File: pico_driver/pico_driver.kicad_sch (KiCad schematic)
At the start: 20 parts, among them J1 GPIO, J2 SRV, J3 ESC, J4 ADC, J5 GP_Breakout, J6 VBUS_OUT, J7 3V3_OUT, J8 FUNC, SW1 SW_SPDT, SW2 SW_Push, SW3 SW_Push, U1 Pico

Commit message: update pcb layout
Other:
- company: (none) -> Engineering Physics - UCA
- title: BearCart - Cerebellum -> BearCart - Driver Board
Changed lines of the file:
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@@
 	(paper "USLetter")
 	(title_block
-		(title "BearCart - Cerebellum")
-		(date "2025-04-25")
-		(rev "0.2")
+		(title "BearCart - Driver Board")
+		(date "2025-05-09")
+		(rev "25.05.001")
+		(company "Engineering Physics - UCA")
 	)
 	(text "Additional pin functions:\nhttps://pinout.xyz/"

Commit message: update schemetic and pcb
Pin header for sw1
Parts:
- SW1: footprint Button_Switch_THT:SW_E-Switch_EG1271_SPDT -> Connector_PinHeader_2.54mm:PinHeader_1x03_P2.54mm_Vertical
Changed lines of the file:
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@@
 			)
 		)
-		(property "Footprint" "Button_Switch_THT:SW_E-Switch_EG1271_SPDT"
+		(property "Footprint" "Connector_PinHeader_2.54mm:PinHeader_1x03_P2.54mm_Vertical"
 			(at 135.89 133.35 0)
 			(effects

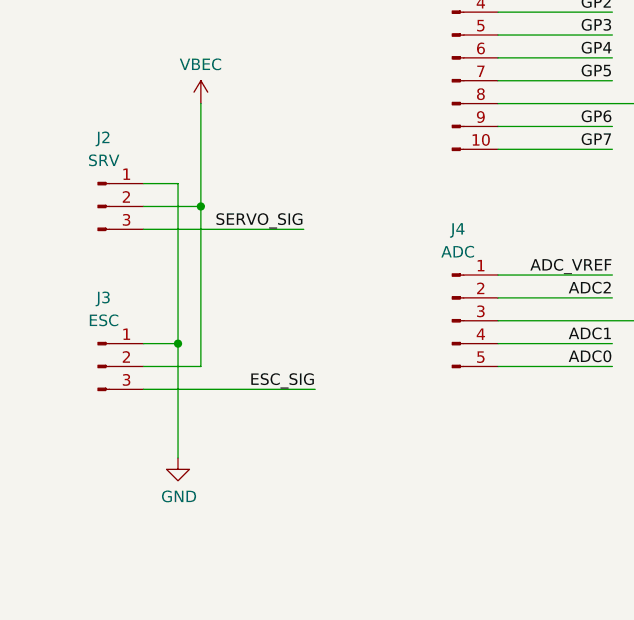
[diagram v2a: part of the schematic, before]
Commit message: update esc and servo pin layout
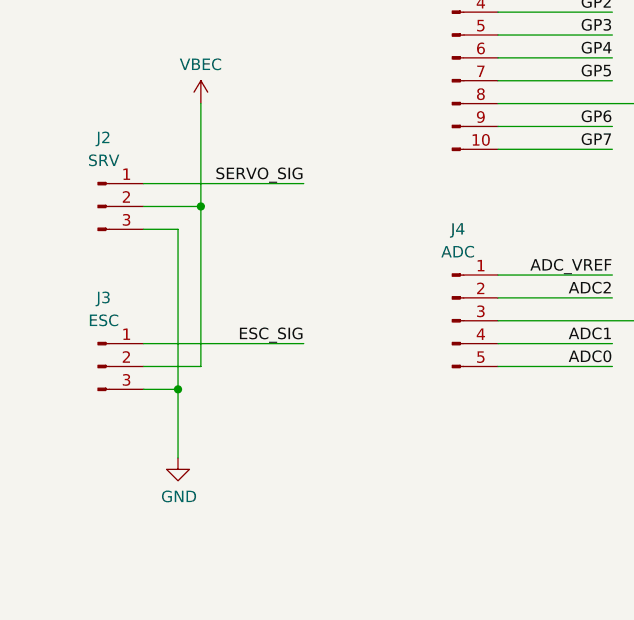
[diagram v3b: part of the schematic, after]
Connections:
- net ESC_SIG: now also J3.1 (Pin_1); no longer J3.3 (Pin_3)
- net GND: now also J2.3 (Pin_3), J3.3 (Pin_3); no longer J2.1 (Pin_1), J3.1 (Pin_1)
- net SERVO_SIG: now also J2.1 (Pin_1); no longer J2.3 (Pin_3)

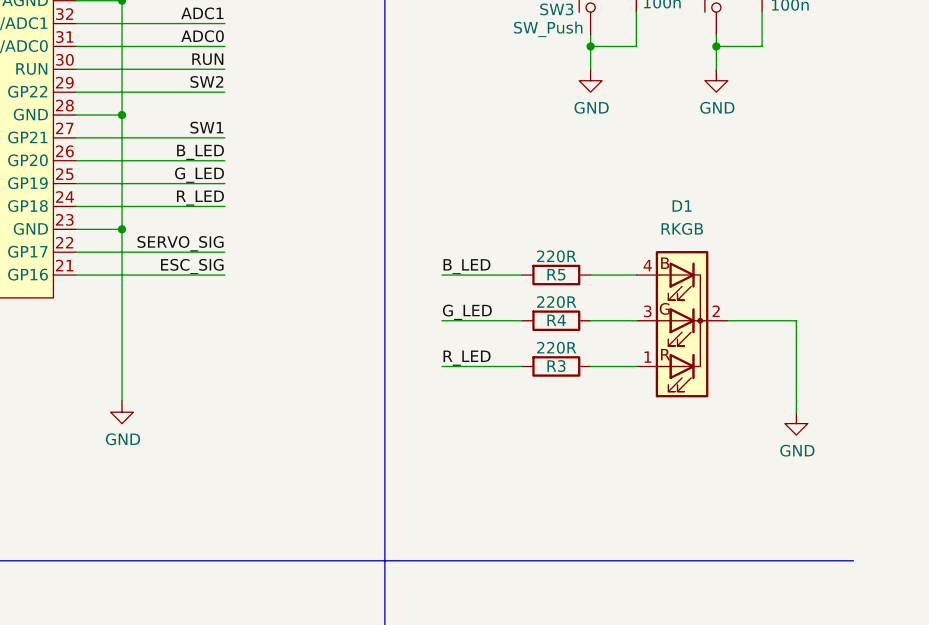
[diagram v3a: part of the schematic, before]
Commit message: update LED footprint
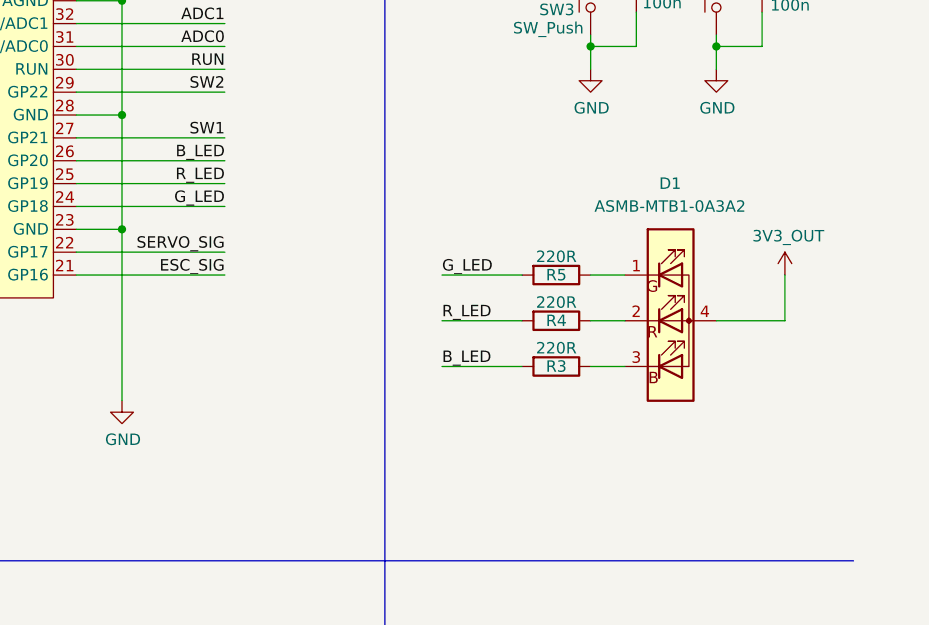
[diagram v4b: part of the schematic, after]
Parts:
- removed D1: RKGB, LED_THT:LED_D5.0mm-4_RGB_Wide_Pins, symbol Device:LED_RKGB
- added D1: ASMB-MTB1-0A3A2, LED_SMD:LED_Avago_PLCC4_3.2x2.8mm_CW, symbol RGB_PLCC4:ASMB-MTB1-0A3A2
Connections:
- net 3V3_OUT: now also D1.4 (A)
- net B_LED: now also R3.2; no longer R5.2
- net G_LED: now also R5.2, U1.24 (GP18); no longer R4.2, U1.25 (GP19)
- net R_LED: now also R4.2, U1.25 (GP19); no longer R3.2, U1.24 (GP18)
- net at R5.1: now also D1.1 (RK)
- net at R4.1: now also D1.2 (GK)
- net at R3.1: now also D1.3 (BK)

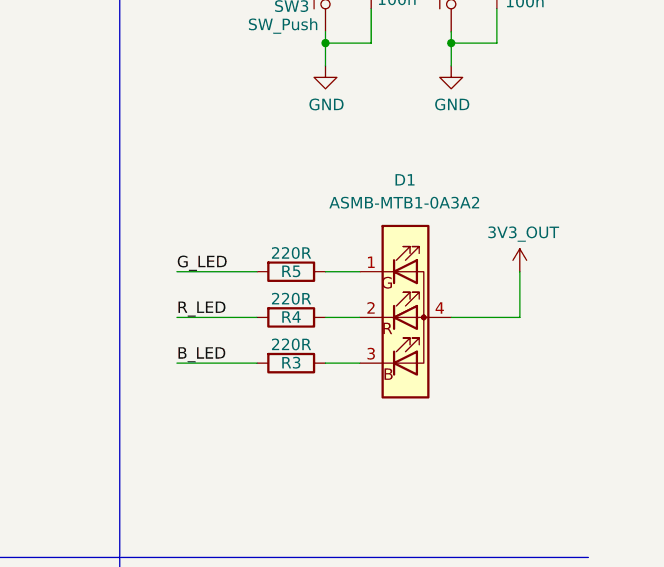
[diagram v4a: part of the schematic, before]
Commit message: update rgb led footprint and layout
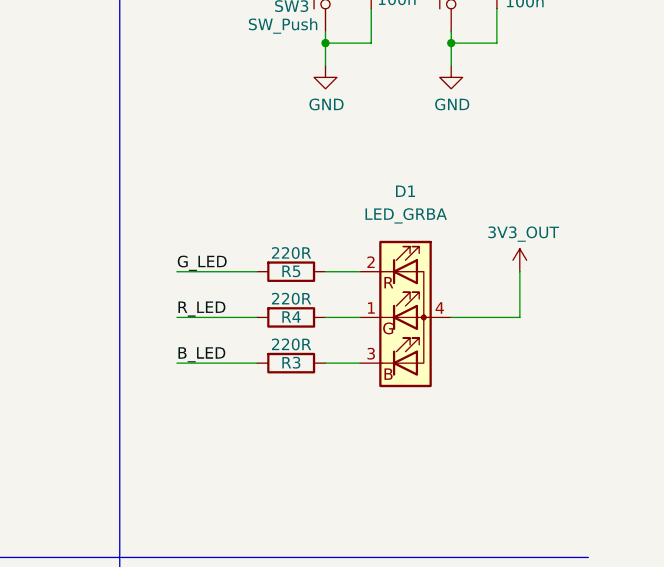
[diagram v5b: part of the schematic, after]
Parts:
- removed D1: ASMB-MTB1-0A3A2, LED_SMD:LED_Avago_PLCC4_3.2x2.8mm_CW, symbol RGB_PLCC4:ASMB-MTB1-0A3A2
- added D1: LED_GRBA, LED_SMD:LED_RGB_1210, symbol Device:LED_GRBA
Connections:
- net 3V3_OUT: now also D1.4 (A)
- net at R5.1: now also D1.2 (RK)
- net at R4.1: now also D1.1 (GK)
- net at R3.1: now also D1.3 (BK)
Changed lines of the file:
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@@
-	)
-	(symbol
-		(lib_id "RGB_PLCC4:ASMB-MTB1-0A3A2")
-		(at 246.38 82.55 0)
-		(unit 1)
-		(exclude_from_sim no)
-		(in_bom yes)
-		(on_board yes)
-		(dnp no)
-		(fields_autoplaced yes)
-		(property "Reference" "D1"
-			(at 246.3244 67.31 0)
-			(effects
-				(font
-					(size 1.27 1.27)
-				)
-			)
-		)
-		(property "Value" "ASMB-MTB1-0A3A2"
-			(at 246.3244 69.85 0)
-			(effects
-				(font
-					(size 1.27 1.27)
-				)
-			)
-		)
-		(property "Footprint" "LED_SMD:LED_Avago_PLCC4_3.2x2.8mm_CW"
-			(at 246.38 67.31 0)
-			(effects
-				(font
-					(size 1.27 1.27)
-				)
-				(hide yes)
-			)
-		)
-		(property "Datasheet" "https://docs.broadcom.com/docs/AV02-4194EN"
-			(at 246.38 93.98 0)
-			(effects
-				(font
-					(size 1.27 1.27)
-				)
-				(hide yes)
-			)
-		)
-		(property "Description" "Tricolor Black Surface LED, Common Anode Pin 4, PLCC-4"
-			(at 246.38 82.55 0)
-			(effects
-				(font
-					(size 1.27 1.27)
-				)
-				(hide yes)
-			)
-		)
-		(pin "2"
-		)
-		(pin "3"
-		)
-		(pin "1"
-		)
-		(pin "4"
-		)
-		(instances
-			(project ""
-				(path "/e63e39d7-6ac0-4ffd-8aa3-1841a4541b55"
-					(reference "D1")
-					(unit 1)
-				)
-			)
-		)
 	)
 	(symbol
@@
 					(unit 1)
 				)
+			)
+		)
+	)
+	(symbol
+		(lib_id "Device:LED_GRBA")
+		(at 246.38 82.55 0)
+		(unit 1)
+		(exclude_from_sim no)
+		(in_bom yes)
+		(on_board yes)
+		(dnp no)
+		(fields_autoplaced yes)
+		(property "Reference" "D1"
+			(at 246.38 68.58 0)
+			(effects
+				(font
+					(size 1.27 1.27)
+				)
+			)
+		)
+		(property "Value" "LED_GRBA"
+			(at 246.38 71.12 0)
+			(effects
+				(font
+					(size 1.27 1.27)
+				)
+			)
+		)
+		(property "Footprint" "LED_SMD:LED_RGB_1210"
+			(at 246.38 83.82 0)
+			(effects
+				(font
+					(size 1.27 1.27)
+				)
+				(hide yes)
+			)
+		)
+		(property "Datasheet" "~"
+			(at 246.38 83.82 0)
+			(effects
+				(font
+					(size 1.27 1.27)
+				)
+				(hide yes)
+			)
+		)
+		(property "Description" "RGB LED, green/red/blue/anode"
+			(at 246.38 82.55 0)
+			(effects
+				(font
+					(size 1.27 1.27)
+				)
+				(hide yes)
+			)
+		)
+		(pin "2"
+		)
+		(pin "3"
+		)
+		(pin "1"
+		)
+		(pin "4"
+		)
+		(instances
+			(project ""
+				(path "/e63e39d7-6ac0-4ffd-8aa3-1841a4541b55"
+					(reference "D1")
+					(unit 1)
+				)
